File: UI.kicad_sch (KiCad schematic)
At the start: 38 parts

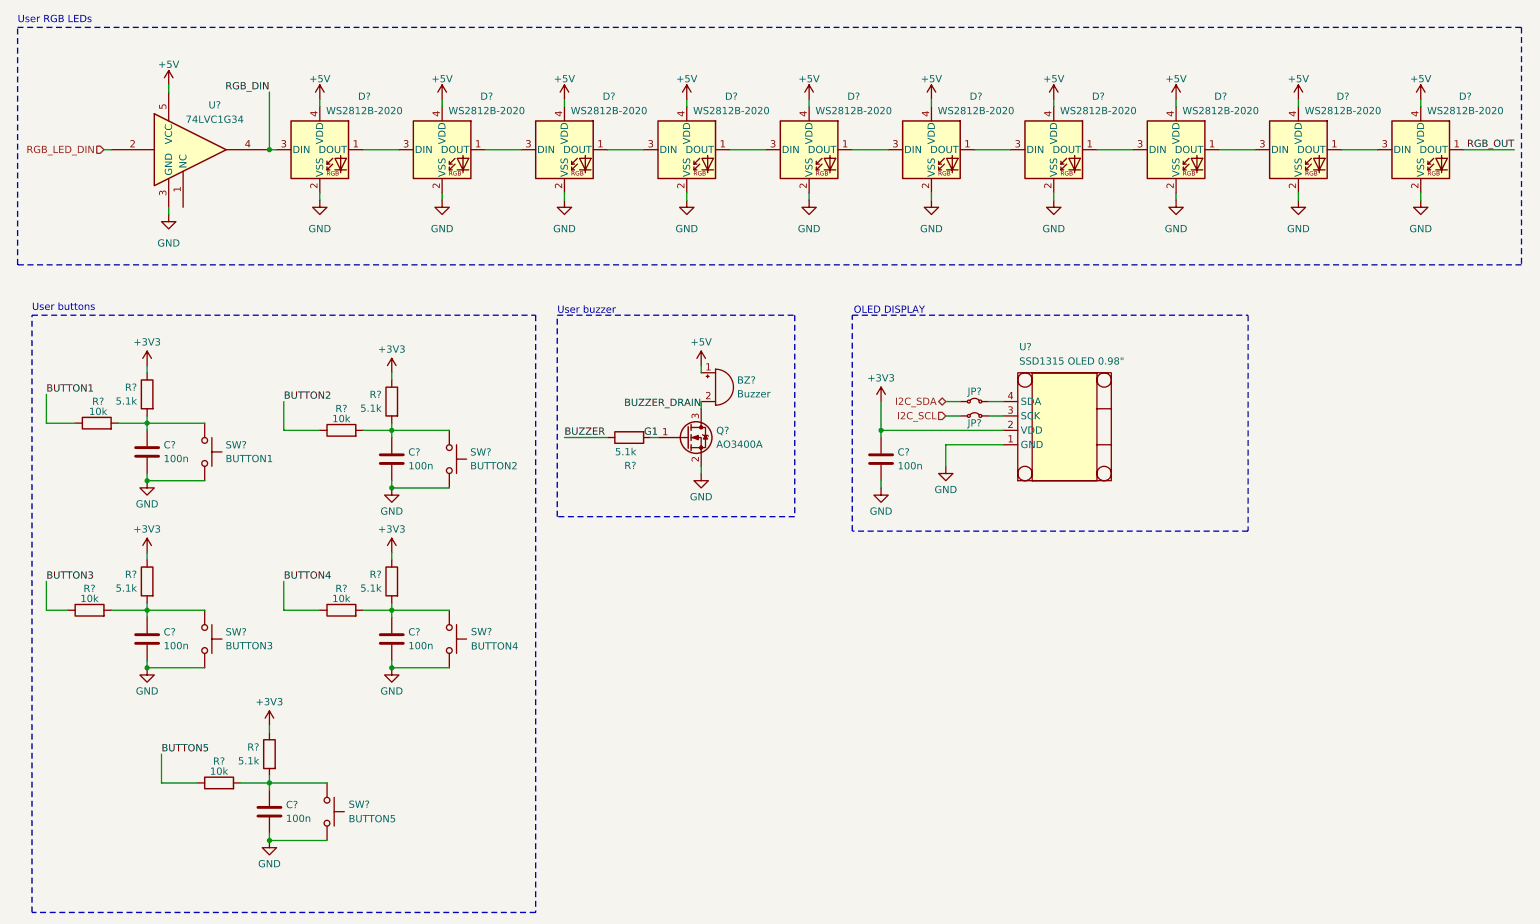
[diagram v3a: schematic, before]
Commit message: Added BME280 on Sensor sheet + Added Power frontend on the dedicated sheet + added I2C Resistors + minor changes
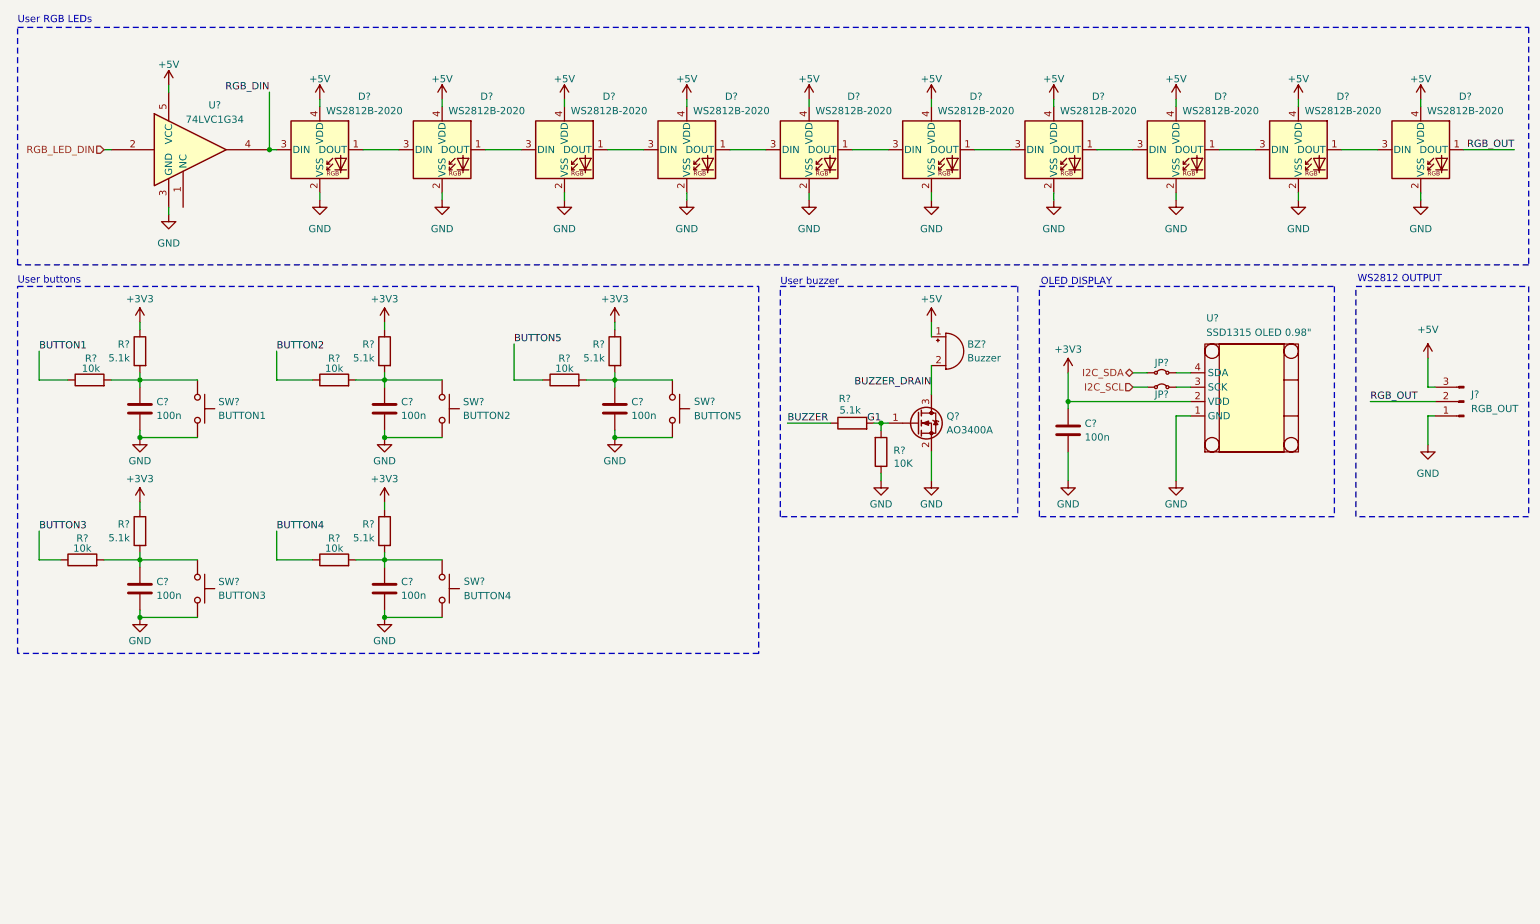
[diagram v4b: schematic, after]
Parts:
- added J?: RGB_OUT, symbol Connector:Conn_01x03_Pin
- added R?: 10K, Resistor_SMD:R_0805_2012Metric_Pad1.20x1.40mm_HandSolder, symbol Device:R
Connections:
- net +5V: now also J?.3 (Pin_3)
- net G1: now also R?.2
- net GND: now also J?.1 (Pin_1), R?.1
- net RGB_OUT: now also J?.2 (Pin_2)
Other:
- note added: "WS2812 OUTPUT"
- moved on the sheet: BZ?, C?, JP?, Q?, R?, SW?, U?

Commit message: Small changes
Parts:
- R?: value 10K -> 100K
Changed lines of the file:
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@@
 			)
 		)
-		(property "Value" "10K"
-			(at 173.228 93.472 0)
+		(property "Value" "100K"
+			(at 174.498 93.472 0)
 			(effects
 				(font

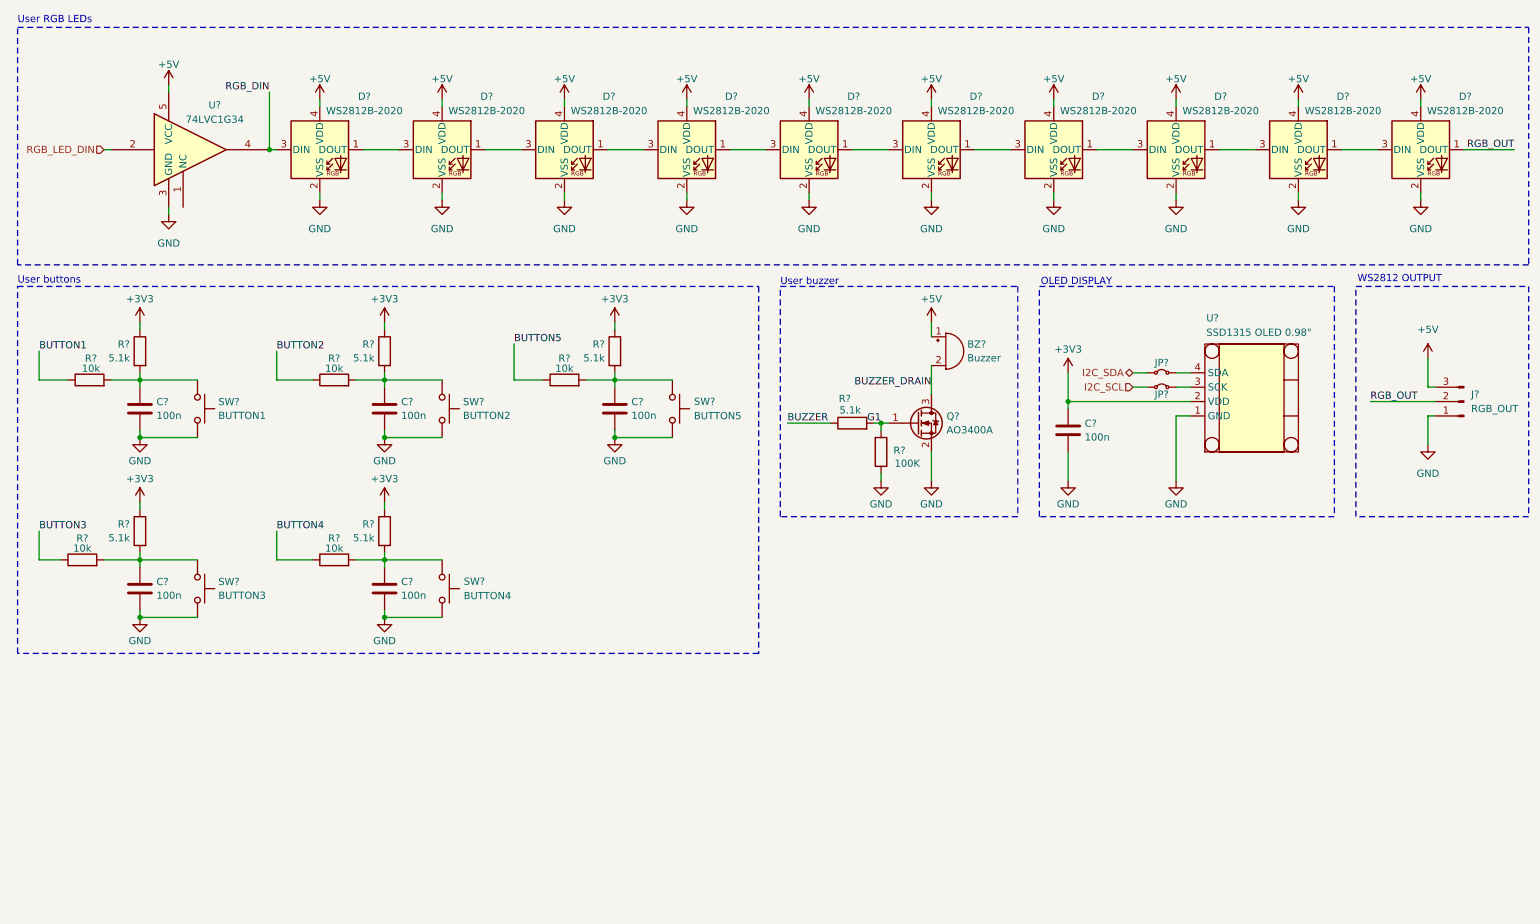
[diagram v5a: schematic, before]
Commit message: Added the hierarchical pins of the sheets and connected them, Fixes #7
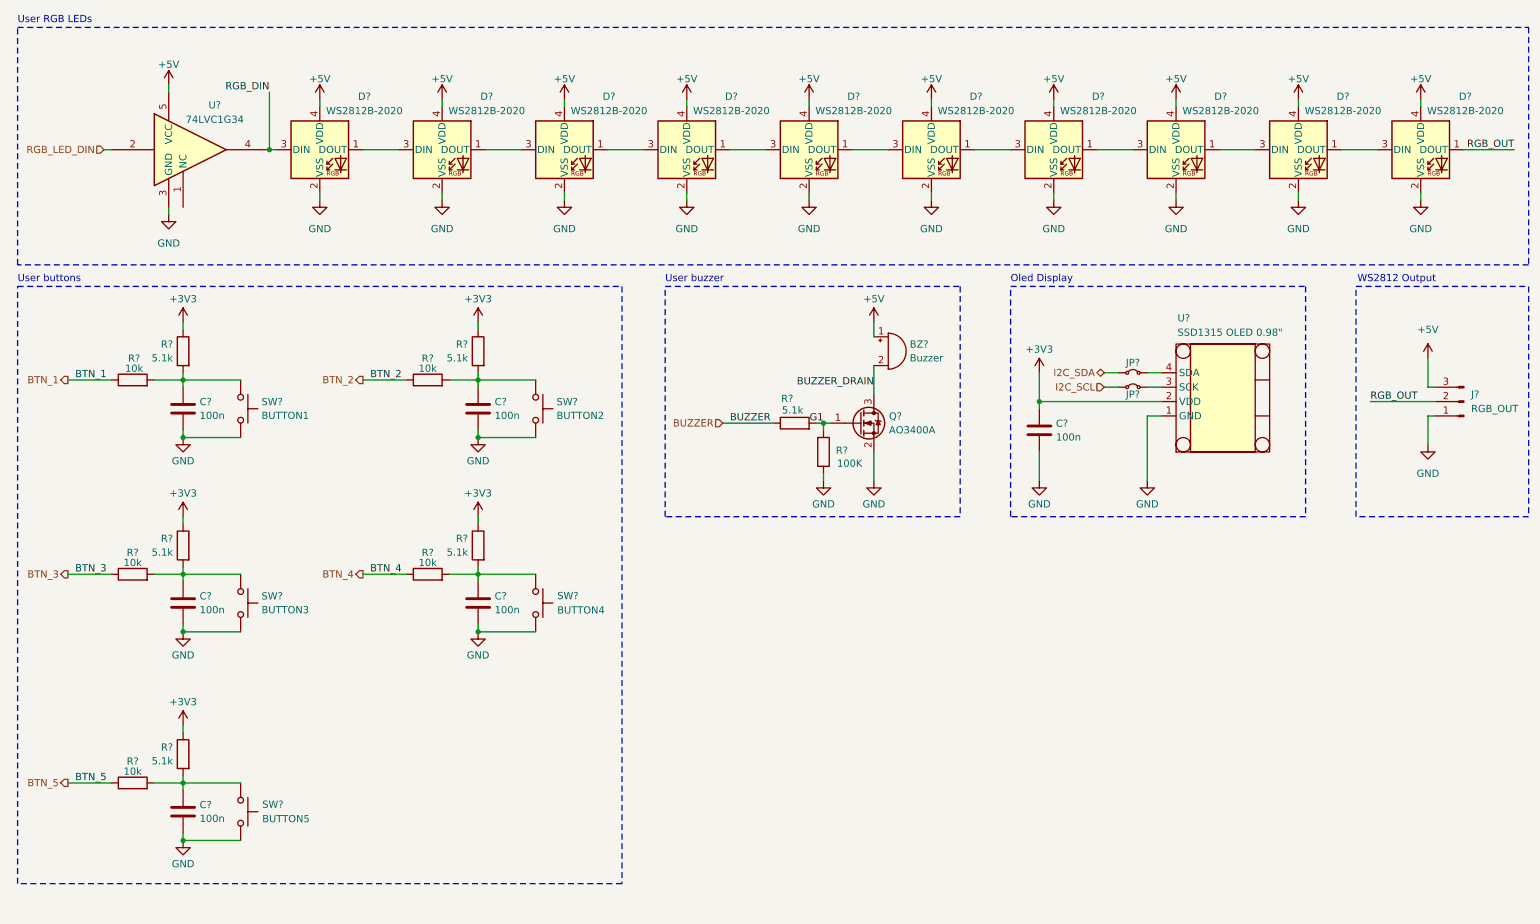
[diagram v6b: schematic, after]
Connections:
- net BUTTON1 renamed BTN_1
- net BUTTON2 renamed BTN_2
- net BUTTON3 renamed BTN_3
- net BUTTON4 renamed BTN_4
- net BUTTON5 renamed BTN_5
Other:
- note added: "Oled Display"
- note added: "WS2812 Output"
- note removed: "OLED DISPLAY"
- note removed: "WS2812 OUTPUT"
- moved on the sheet: BZ?, C?, JP?, Q?, R?, SW?, U?
